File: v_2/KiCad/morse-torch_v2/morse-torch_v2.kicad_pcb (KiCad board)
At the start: 2 copper layers, 58.9 x 70 mm, 38 parts, among them J2 USART, J3 I2C, J4 AVR-ISP-6, J5 LIGHT, J6 BATT, J7 PWR, Q1 BC817, SW1 SW_Push, SW2 SW_Push, SW3 Rotary_Encoder_Switch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

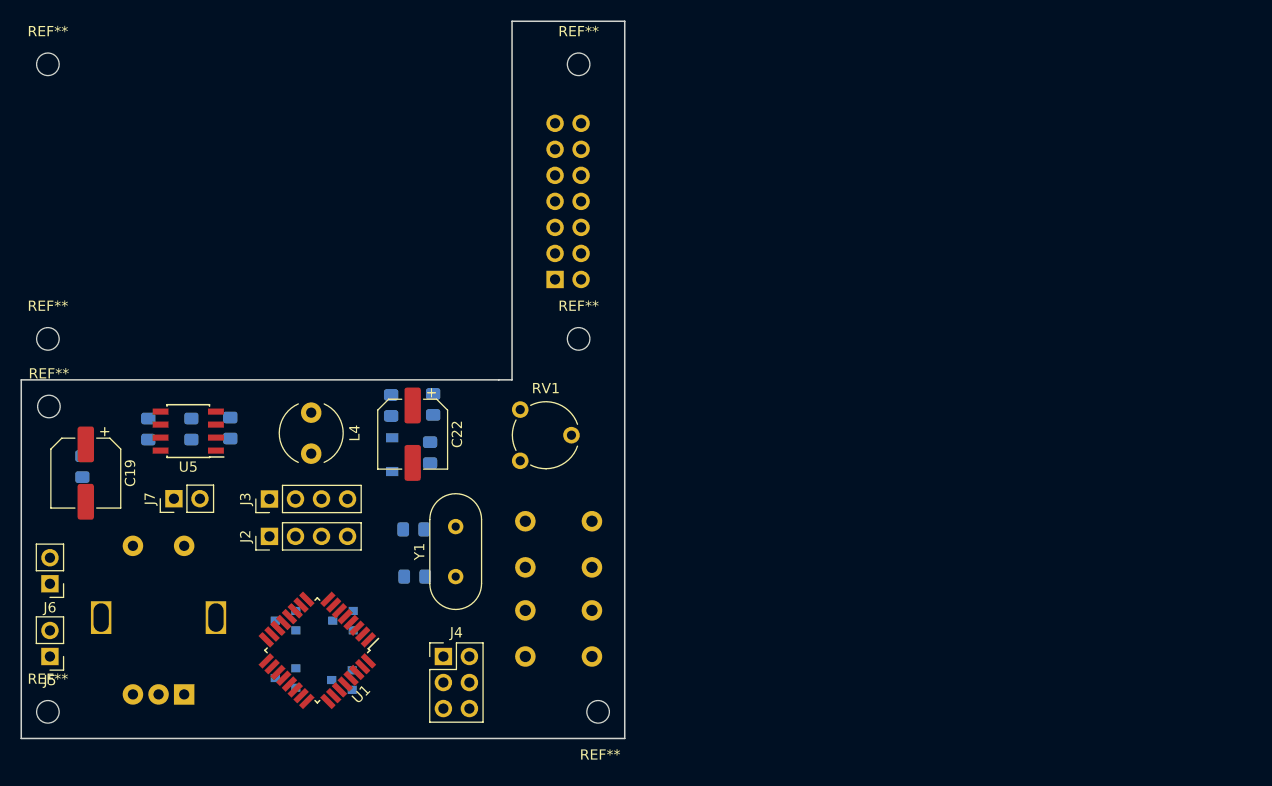
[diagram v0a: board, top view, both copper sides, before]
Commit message: changed uc to atmega32, added jtag interface, roughly set up final layout
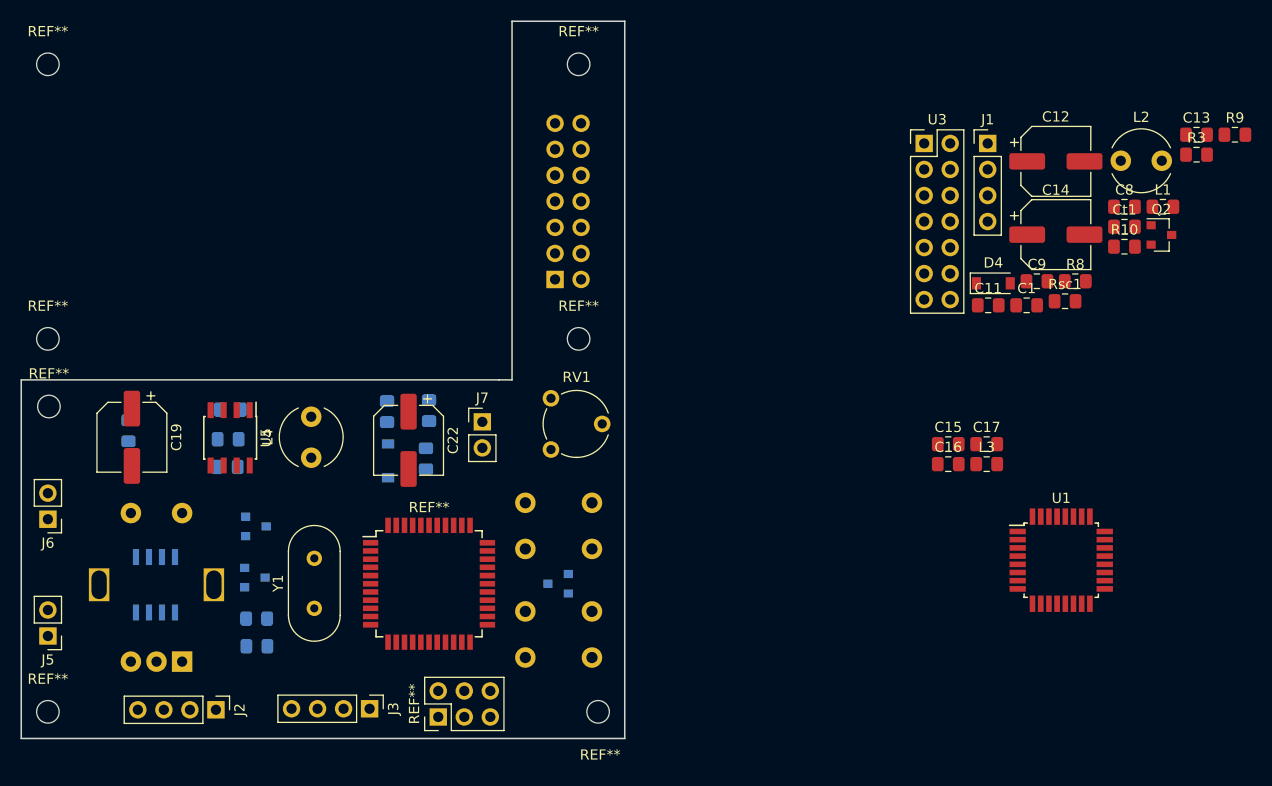
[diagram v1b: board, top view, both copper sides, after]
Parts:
- removed D3: BAT54C, Package_TO_SOT_SMD:SOT-23
- removed J4: AVR-ISP-6, Connector_PinHeader_2.54mm:PinHeader_2x03_P2.54mm_Vertical
- added C1: 100nF, Capacitor_SMD:C_0805_2012Metric_Pad1.15x1.40mm_HandSolder, F.Cu at (210.5, 84.4)
- added C11: 100n, Capacitor_SMD:C_0805_2012Metric_Pad1.15x1.40mm_HandSolder, F.Cu at (206.8, 84.4)
- added C12: 100u, Capacitor_SMD:CP_Elec_6.3x5.4, F.Cu at (213.4, 70.4)
- added C13: 100n, Capacitor_SMD:C_0805_2012Metric_Pad1.15x1.40mm_HandSolder, F.Cu at (227.1, 67.8)
- added C14: 100u, Capacitor_SMD:CP_Elec_6.3x5.4, F.Cu at (213.4, 77.5)
- added C15: 100nF, Capacitor_SMD:C_0805_2012Metric_Pad1.15x1.40mm_HandSolder, F.Cu at (202.9, 98.0)
- added C16: 100nF, Capacitor_SMD:C_0805_2012Metric_Pad1.15x1.40mm_HandSolder, F.Cu at (202.9, 99.9)
- added C17: 100nF, Capacitor_SMD:C_0805_2012Metric_Pad1.15x1.40mm_HandSolder, F.Cu at (206.6, 98.0)
- added C8: 22pF, Capacitor_SMD:C_0805_2012Metric_Pad1.15x1.40mm_HandSolder, F.Cu at (220.1, 74.8)
- added C9: 22pF, Capacitor_SMD:C_0805_2012Metric_Pad1.15x1.40mm_HandSolder, F.Cu at (211.5, 82.1)
- added Ct1: 470p, Capacitor_SMD:C_0805_2012Metric_Pad1.15x1.40mm_HandSolder, F.Cu at (220.1, 76.8)
- added D4: MBR0520, Diode_SMD:D_SOD-123, F.Cu at (207.3, 82.3)
- added J1: USART, Connector_PinHeader_2.54mm:PinHeader_1x04_P2.54mm_Vertical, F.Cu at (206.7, 68.6)
- added L1: 10uH, Inductor_SMD:L_0805_2012Metric_Pad1.15x1.40mm_HandSolder, F.Cu at (223.8, 74.8)
- added L2: 82u, Inductor_THT:L_Radial_D6.0mm_P4.00mm, F.Cu at (219.7, 70.3)
- added L3: 10uH, Inductor_SMD:L_0805_2012Metric_Pad1.15x1.40mm_HandSolder, F.Cu at (206.6, 99.9)
- added Q2: BC817, Package_TO_SOT_SMD:SOT-23, F.Cu at (223.7, 77.6)
- added R10: 390k, Resistor_SMD:R_0805_2012Metric_Pad1.15x1.40mm_HandSolder, F.Cu at (220.1, 78.7)
- added R3: 10k, Resistor_SMD:R_0805_2012Metric_Pad1.15x1.40mm_HandSolder, F.Cu at (227.1, 69.7)
- added R8: 130k, Resistor_SMD:R_0805_2012Metric_Pad1.15x1.40mm_HandSolder, F.Cu at (215.3, 82.1)
- added R9: 100k, Resistor_SMD:R_0805_2012Metric_Pad1.15x1.40mm_HandSolder, F.Cu at (230.9, 67.8)
- added REF**: TQFP-44_10x10mm_P0.8mm, Package_QFP:TQFP-44_10x10mm_P0.8mm, F.Cu at (152.2, 111.6)
- added REF**: , Connector_PinHeader_2.54mm:PinHeader_2x03_P2.54mm_Vertical, F.Cu at (153.1, 124.6)
- added Rsc1: 1, Resistor_SMD:R_0805_2012Metric_Pad1.15x1.40mm_HandSolder, F.Cu at (214.3, 84.0)
- added U2: 24LC128, Package_SO:SOIC-8_3.9x4.9mm_P1.27mm, B.Cu at (125.5, 111.7)
- added U3: NHD-0420H1Z, Connector_PinHeader_2.54mm:PinHeader_2x07_P2.54mm_Vertical, F.Cu at (200.5, 68.6)
- C4, C5: value 22pF -> 100nF
- J2: value USART -> AVR-ISP-6
- J6: value BATT -> PWR
- J7: value PWR -> Microsemi_FlashPro-JTAG-10
- R11: value 1 -> 10k
- U4: value NHD-0420H1Z -> MC34063AD
- U5: value MC34063AD -> ATmega32-16AU
- moved U1 73.1 mm to (213.9, 109.3), turned to 0 degrees
- moved J7 31.0 mm to (157.4, 95.8), turned to 0 degrees
- moved J3 22.7 mm to (146.4, 123.8), turned to 270 degrees
- moved D1 21.3 mm to (164.8, 111.6)
- moved J2 17.7 mm to (131.4, 123.9), turned to 270 degrees
- moved C5 17.6 mm to (135.4, 115.0)
- moved C4 16.8 mm to (135.4, 117.7)
- moved Q1 15.1 mm to (135.3, 106.0), turned to 0 degrees
- moved Y1 14.1 mm to (141.0, 114.0)
- moved R11 8.54 mm to (132.5, 100.2), turned to 180 degrees
- moved J6 6.30 mm to (115.0, 105.3)
- moved C18 5.70 mm to (122.9, 96.7)
- moved C19 5.70 mm to (123.2, 97.3)
- moved D2 5.16 mm to (135.2, 111.0), turned to 0 degrees
- moved L4 4.40 mm to (140.7, 99.3), turned to 90 degrees
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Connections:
- C4 pad 1: XTAL1 -> +5V
- C5 pad 1: XTAL2 -> Net-(C5-Pad1)
- J2 pad 1: GND -> MISO
- J2 pad 3: TXD -> SCK
- J2 pad 4: RXD -> MOSI
- J5 pad 1: LIGHT_VCC -> Net-(J5-Pad1)
- J5 pad 2: GND -> ADC0
- J6 pad 1: ADC0 -> Net-(C11-Pad1)
- J6 pad 2: GND -> ADC0
- J7 pad 1: +5V -> Net-(J7-Pad1)
- J7 pad 2: 5V-converter -> Net-(J7-Pad10)
- Q1 pad 2: LIGHT_VCC -> GND
- Q1 pad 3: +5V -> Net-(Q1-Pad3)
- R11 pad 1: Net-(L4-Pad1) -> +5V
- R11 pad 2: ADC0 -> RESET
- U1 pad 1: Net-(U1-Pad1) -> write-protection
- U4 pad 1: GND -> Net-(D4-Pad2)
- U4 pad 10: LCD_DATA3 -> (no net)
- U4 pad 11: LCD_DATA4 -> (no net)
- U4 pad 12: LCD_DATA5 -> (no net)
- U4 pad 13: LCD_DATA6 -> (no net)
- U4 pad 14: LCD_DATA7 -> (no net)
- U4 pad 2: +5V -> GND
- U4 pad 3: Net-(RV1-Pad2) -> Net-(Ct1-Pad1)
- U4 pad 4: LCD_RS -> GND
- U4 pad 5: GND -> Net-(R10-Pad1)
- U4 pad 6: LCD_E -> Net-(C11-Pad1)
- U4 pad 7: LCD_DATA0 -> Net-(L2-Pad1)
- U4 pad 8: LCD_DATA1 -> Net-(R9-Pad2)
- U4 pad 9: LCD_DATA2 -> (no net)
- U5 pad 1: Net-(D12-Pad2) -> Net-(U5-Pad1)
- U5 pad 2: GND -> Net-(U5-Pad2)
- U5 pad 3: Net-(C20-Pad1) -> Net-(U5-Pad3)
- U5 pad 4: GND -> RESET
- U5 pad 5: Net-(R12-Pad2) -> +5V
- U5 pad 6: ADC0 -> Net-(U5-Pad18)
- U5 pad 7: Net-(L4-Pad1) -> XTAL2
- U5 pad 8: Net-(R13-Pad2) -> XTAL1
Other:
- board text added: "->"
- board text added: "czy wystajace headery sie zmieszcza? ->"
- board text added: "sprawdzic orientacje ->"
